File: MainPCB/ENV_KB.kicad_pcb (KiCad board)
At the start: 2 copper layers, 354.6 x 156.5 mm, 198 parts, among them J0 TYPE-C-31-M-12

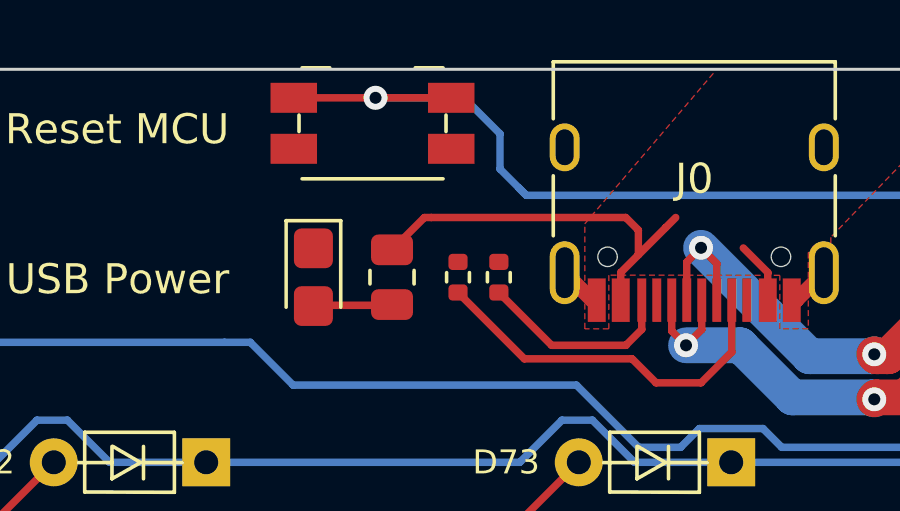
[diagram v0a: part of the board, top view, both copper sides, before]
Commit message: Changed Button to B3U from EVQ + smaller LED resistor
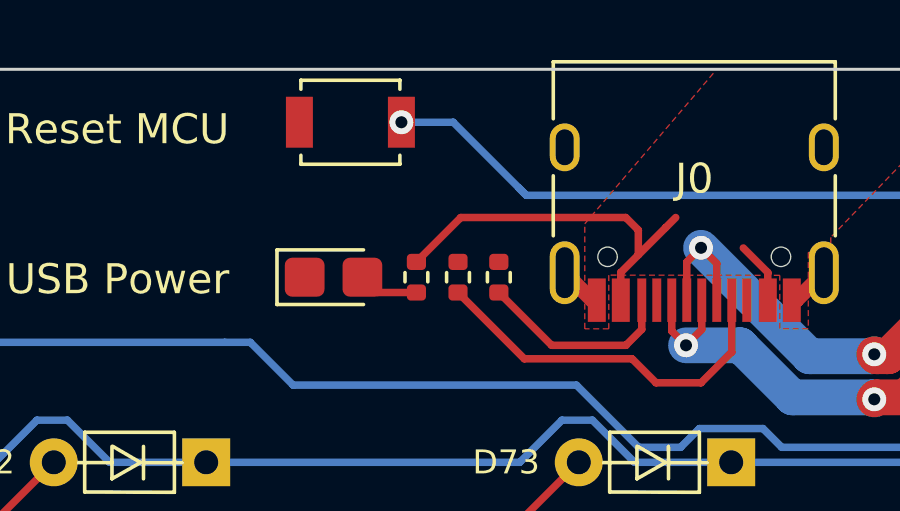
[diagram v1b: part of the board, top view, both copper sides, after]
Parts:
- PowerLedResistor0: footprint Resistor_SMD:R_0805_2012Metric -> Resistor_SMD:R_0402_1005Metric
- SW-RST0: footprint Button_Switch_SMD:Panasonic_EVQPUJ_EVQPUA -> Button_Switch_SMD:SW_SPST_B3U-1000P
- moved PowerLedResistor0 0.81 mm to (202.9, 66.6)
- moved SW-RST0 0.74 mm to (200.7, 61.4), turned to 180 degrees
- moved PowerLED0 0.67 mm to (200.2, 66.6), turned to 0 degrees
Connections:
- J0 pad A8: Net-(J0-PadA8) -> (no net)
- J0 pad B8: Net-(J0-PadB8) -> (no net)
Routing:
- net Resetbtn: track 78.6 -> 71.4 mm
- net USBVBUS: track 15.2 -> 14.6 mm
- net Net-(PowerLED0-Pad2): track 2.60 -> 2.01 mm

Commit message: Re aligned all diodes and re-did traces for all diodes
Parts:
- removed H8: MountingHole, MountingHole:MountingHole_3.2mm_M3
- D0, D1, D10, D11, D12, D13, D14, D15, D16, D17, D18, D19, D2, D20, D21, D22, D23, D24, D25, D26, D27, D28, D29, D3, D30, D31, D32, D33, D34, D35, D36, D37, D38, D39, D4, D40, D41, D42, D43, D44, D45, D46, D47, D48, D49, D5, D50, D51, D52, D53, D54, D55, D56, D57, D58, D59, D6, D60, D61, D62, D63, D64, D65, D66, D67, D68, D69, D7, D70, D71, D72, D73, D74, D75, D76, D77, D78, D79, D8, D80, D81, D82, D83, D84, D85, D86, D87, D88, D9: footprint CFTKB Bits:D_DO-35_SOD27_P5.08mm_Horizontal -> Diode_THT:D_DO-35_SOD27_P7.62mm_Horizontal
- PowerLED0: value Green Power Led -> LED 0805; footprint LED_SMD:LED_0805_2012Metric_Castellated -> LED_SMD:LED_0402_1005Metric
- PowerLedResistor0: value 1K Resistor -> 1K Resistor 0402
- RESISTOR0, RESISTOR1: value 5.1kohm -> 5.1kohm 0402
- SW-RST0: value Reset Buton -> B3U-1000
- moved D78 8.03 mm to (49.2, 69.7)
- moved D0 7.93 mm to (49.3, 89.7)
- moved D16 7.93 mm to (49.3, 85.7)
- moved D33 7.93 mm to (49.3, 81.7)
- moved D50 7.93 mm to (49.3, 77.7)
- moved D64 7.93 mm to (49.3, 73.7)
- moved D17 7.33 mm to (67.4, 85.7)
- moved D65 7.33 mm to (67.4, 73.7)
- moved D79 7.33 mm to (67.4, 69.7)
- moved D1 6.74 mm to (85.5, 89.7)
- moved D18 6.74 mm to (85.5, 85.7)
- moved D34 6.74 mm to (85.5, 81.7)
- moved D51 6.74 mm to (85.5, 77.7)
- moved D66 6.74 mm to (85.5, 73.7)
- moved D19 6.15 mm to (103.6, 85.7)
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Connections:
- J0 pad A8: (no net) -> Net-(J0-PadA8)
- J0 pad B8: (no net) -> Net-(J0-PadB8)
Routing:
- net row6: track 363.7 -> 379.2 mm
- net Net-(D15-Pad2): track 8.78 -> 17.2 mm
- net GND: track 5.38 -> 13.0 mm
- net Net-(D78-Pad2): track 142.4 -> 149.0 mm
- net Net-(D16-Pad2): track 43.9 -> 50.2 mm
- net Net-(D33-Pad2): track 66.2 -> 72.4 mm
- net Net-(D50-Pad2): track 91.9 -> 98.1 mm
- net Net-(D64-Pad2): track 124.6 -> 130.8 mm
- net Net-(D18-Pad2): track 51.3 -> 45.3 mm
- net Net-(D4-Pad2): track 10.5 -> 16.2 mm
- net Net-(D3-Pad2): track 10.9 -> 16.5 mm
- net Net-(D14-Pad2): track 9.82 -> 15.2 mm
- net row5: track 347.8 -> 353.0 mm
- net Net-(D7-Pad2): track 9.28 -> 14.0 mm
- net Net-(D17-Pad2): track 49.6 -> 45.2 mm
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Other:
- board size 354.6 x 156.5 mm -> 354.6 x 156.1 mm
- board text added: "PLEASE CHECK ALIGNMENT OF "TYPE-C-31-M-12" or "J0""
- board text removed: "3.3V"
- board text removed: ">"
- board text removed: "GND"
- board text removed: "LOL"
- board text removed: "PLEASE CHECK ALIGNMENT OF USB TYPE C PORT"
- board text removed: "SCL"
- board text removed: "This scale is 10CM long"

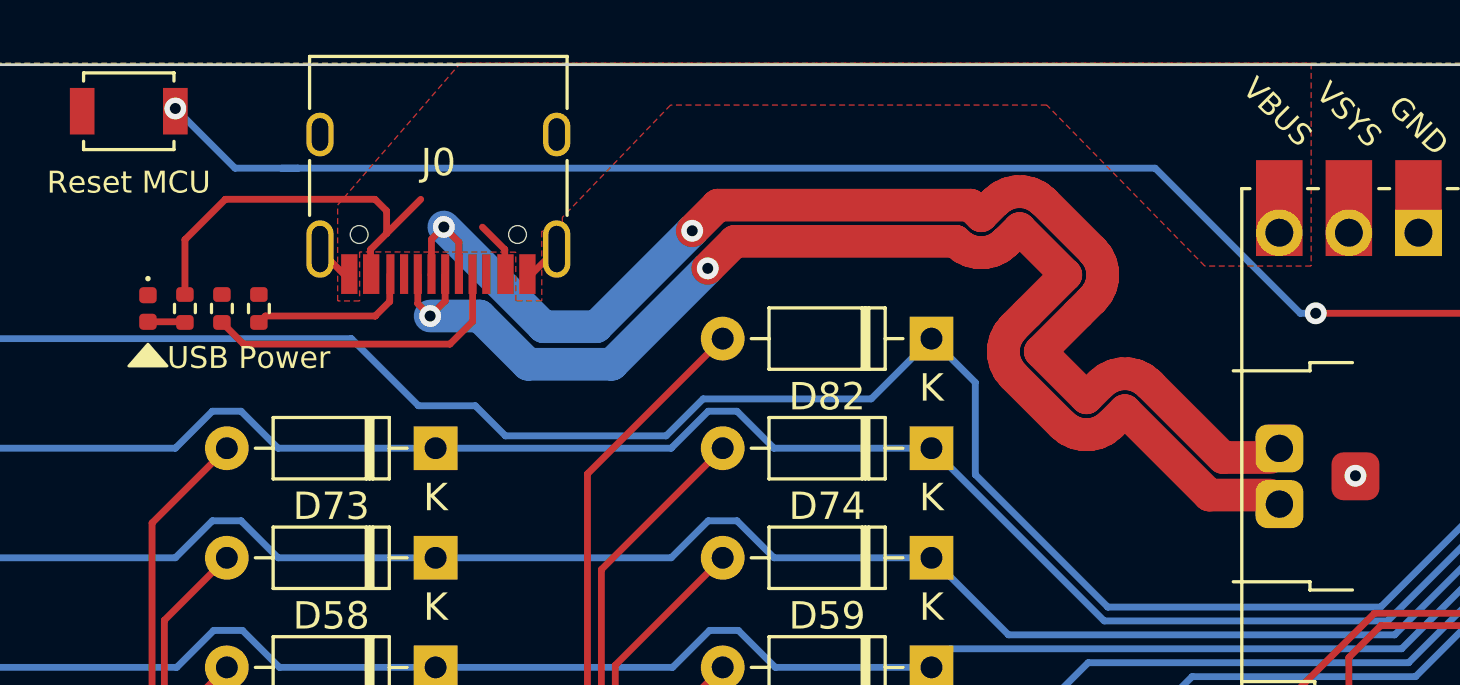
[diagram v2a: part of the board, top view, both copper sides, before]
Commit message: changed type-c port and re-did some bits
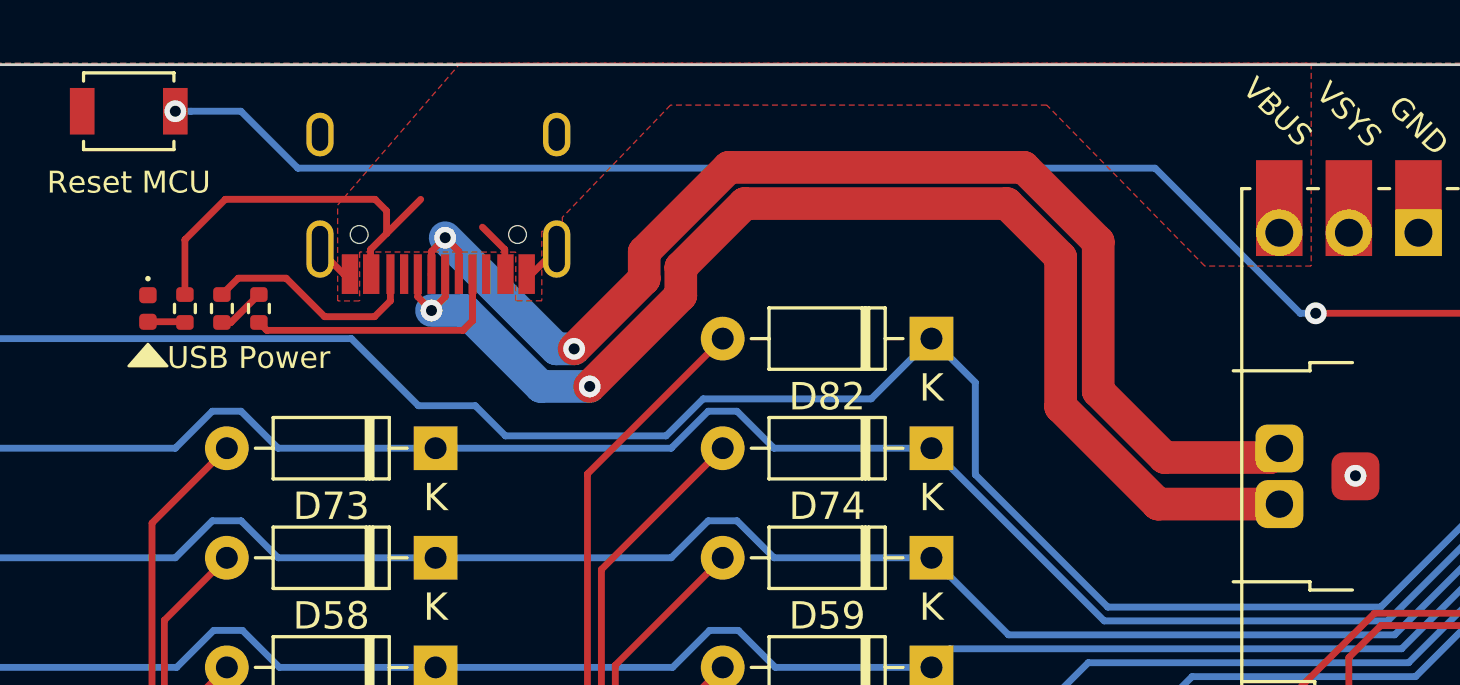
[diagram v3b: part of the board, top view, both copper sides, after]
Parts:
- removed J0: TYPE-C-31-M-12, EM_Extras:USB_C_Receptacle_HRO_TYPE-C-31-M-12
- added USB1: HRO-TYPE-C-31-M-12, HRO-TYPE-C31-M-12:HRO-TYPE-C-31-M-12, F.Cu at (212.2, 59.6)
- PowerLED0: value LED 0805 -> LED 0402
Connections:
- RESISTOR0 pad 1: GND -> Net-(RESISTOR0-Pad1)
- RESISTOR0 pad 2: Net-(J0-PadA5) -> GND
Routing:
- net Net-(J0-PadA5): track 11.5 -> 0.00 mm
- net Net-(RESISTOR0-Pad1): track 0.00 -> 8.20 mm
- net Net-(RESISTOR1-Pad2): track 6.07 -> 9.77 mm
- net GND: track 13.0 -> 14.7 mm
- net USB2_N: track 48.0 -> 46.3 mm
- net USB2_P: track 47.3 -> 46.3 mm
- net Resetbtn: track 71.6 -> 71.0 mm
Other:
- board text added: "PLEASE CHECK ALIGNMENT OF "HRO-TYPE-C-31-M-12""
- board text removed: "PLEASE CHECK ALIGNMENT OF "TYPE-C-31-M-12" or "J0""

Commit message: adjusted traces, placements and clearances on main PCB and re-generated Gerber, Bom and Position file
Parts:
- moved PowerLED0 1.80 mm to (199.8, 68.6)
- moved RESISTOR1 1.80 mm to (203.9, 68.6)
- moved PowerLedResistor0 1.80 mm to (201.2, 68.6)
- moved RESISTOR0 1.80 mm to (202.5, 68.6)
- moved D61 1.05 mm to (319.0, 74.6)
- moved D62 1.05 mm to (331.6, 74.6)
- moved D63 1.05 mm to (344.1, 74.6)
- moved D10 1.05 mm to (319.0, 86.4)
- moved D11 1.05 mm to (331.6, 86.4)
- moved D12 1.05 mm to (344.1, 86.4)
- moved D13 1.05 mm to (356.7, 86.4)
- moved D15 1.05 mm to (381.8, 86.4)
- moved D28 1.05 mm to (319.0, 82.5)
- moved D29 1.05 mm to (344.1, 82.5)
- moved D30 1.05 mm to (356.7, 82.5)
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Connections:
- USB1 pad 11: VBUS -> USBVBUS
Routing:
- net USBVBUS: track 16.6 -> 31.2 mm
- net row6: track 379.2 -> 369.2 mm
- net GND: track 14.7 -> 5.70 mm, vias 2 -> 4
- net Net-(RESISTOR1-Pad2): track 9.77 -> 11.9 mm
- net Net-(D47-Pad2): track 97.8 -> 95.7 mm
- net row2: track 376.1 -> 374.1 mm
- net Net-(RESISTOR0-Pad1): track 8.20 -> 10.1 mm
- net Net-(D3-Pad2): track 16.5 -> 18.2 mm
- net Net-(D48-Pad2): track 128.3 -> 126.6 mm
- net Net-(D49-Pad2): track 158.7 -> 157.1 mm
- net Net-(D30-Pad2): track 73.1 -> 71.6 mm
- net Net-(D87-Pad2): track 196.3 -> 197.8 mm
- net Net-(D13-Pad2): track 17.3 -> 16.1 mm
- net Net-(D31-Pad2): track 102.5 -> 101.3 mm
- net Net-(D32-Pad2): track 133.0 -> 131.8 mm
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
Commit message: some small alignment tweaks and corrections
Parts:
- K_0, K_1, K_10, K_11, K_12, K_13, K_14, K_15, K_16, K_17, K_18, K_19, K_2, K_20, K_21, K_22, K_23, K_24, K_25, K_26, K_27, K_28, K_3, K_30, K_31, K_32, K_34, K_35, K_36, K_37, K_38, K_39, K_4, K_40, K_41, K_42, K_43, K_44, K_45, K_47, K_48, K_49, K_5, K_51, K_52, K_53, K_54, K_55, K_56, K_57, K_58, K_59, K_6, K_60, K_61, K_62, K_65, K_66, K_67, K_68, K_69, K_7, K_70, K_71, K_72, K_73, K_74, K_75, K_77, K_8, K_86, K_87, K_88, K_9: footprint MX_only:MXOnly-1U-NoLED -> MX_Only:MXOnly-1U-NoLED
- K_29: footprint MX_only:MXOnly-2U-NoLED -> MX_Only:MXOnly-2U-NoLED
- K_33, K_46: footprint MX_only:MXOnly-1.5U-NoLED -> MX_Only:MXOnly-1.5U-NoLED
- K_50: footprint MX_only:MXOnly-1.75U-NoLED -> MX_Only:MXOnly-1.75U-NoLED
- K_63B1, K_64B1: footprint MX_only:MXOnly-2.25U-NoLED -> MX_Only:MXOnly-2.25U-NoLED
- K_64, K_78, K_79, K_80, K_82, K_83, K_84, K_85: footprint MX_only:MXOnly-1.25U-NoLED -> MX_Only:MXOnly-1.25U-NoLED
- K_76: footprint MX_only:MXOnly-2.75U-NoLED -> MX_Only:MXOnly-2.75U-NoLED
- K_81: footprint MX_only:MXOnly-6.25U-ReversedStabilizers-NoLED -> MX_Only:MXOnly-6.25U-ReversedStabilizers-NoLED

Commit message: Changed Logo and fixed missing silkscreen for I2C header
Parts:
- removed the G*** at (356.2, 168.3)
- added G***: LOGO, EM_Logo:KBLogo, F.Cu at (357.1, 168.5)
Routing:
- net GND: vias 4 -> 5
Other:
- board text added: "3V3"
- board text added: "GND"
- board text added: "SCL"
